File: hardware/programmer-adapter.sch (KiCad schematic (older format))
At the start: 5 parts, among them J2 Target, J3 Conn_ARM_JTAG_SWD_20, U1 AMS1117-3.3

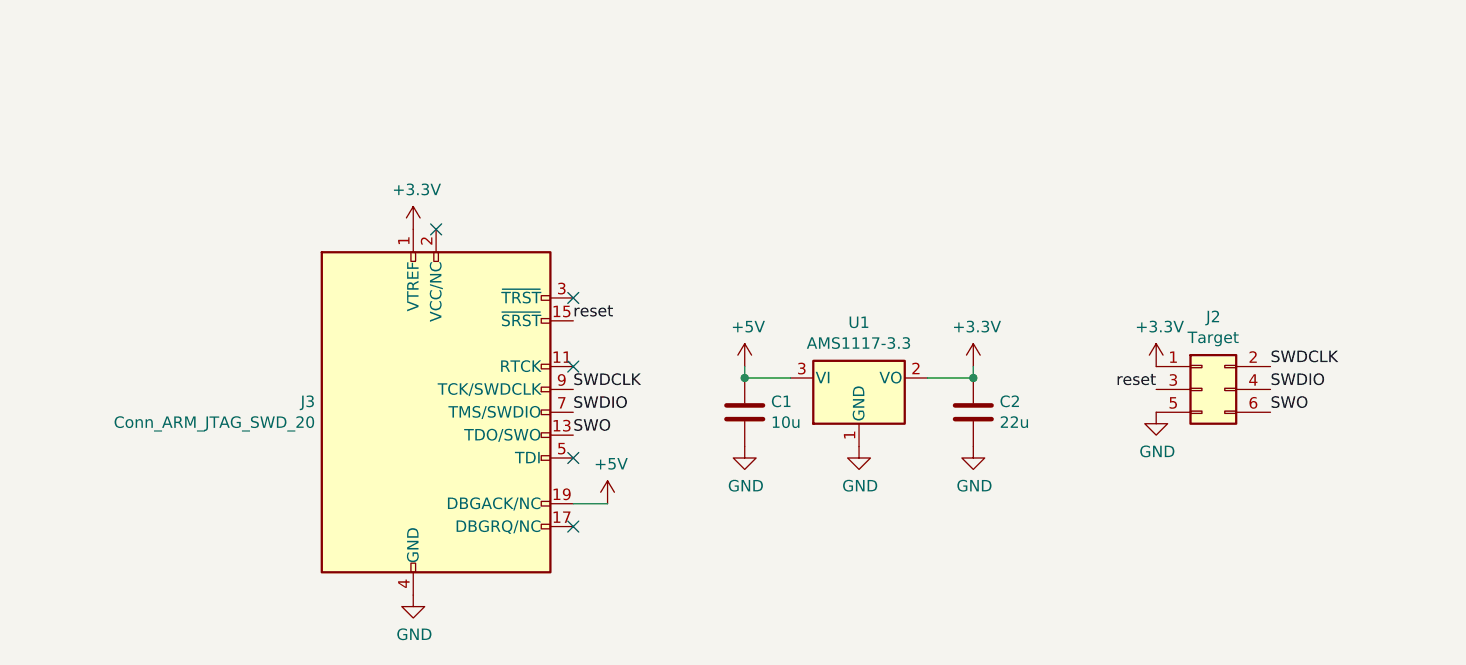
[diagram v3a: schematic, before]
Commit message: Changed LDO to MCP1826S
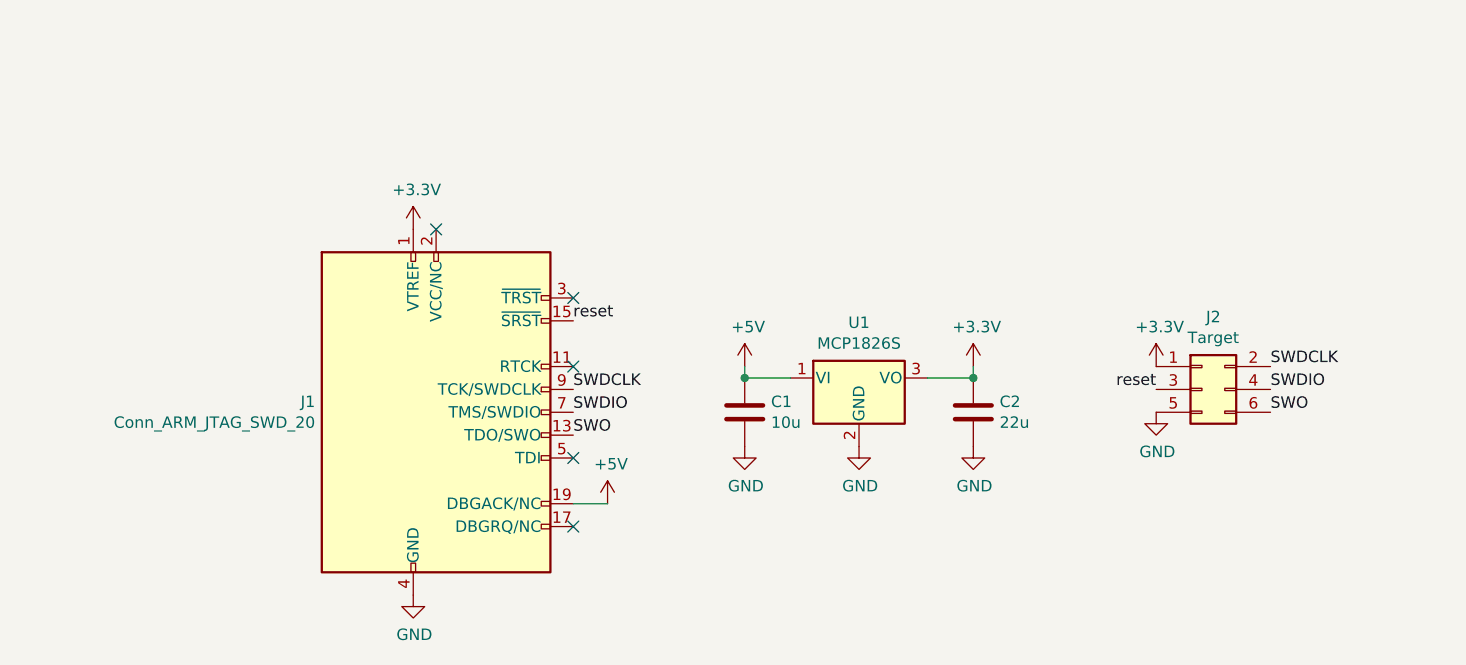
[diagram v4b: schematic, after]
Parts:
- removed U1: AMS1117-3.3, Package_TO_SOT_SMD:SOT-223-3_TabPin2, symbol Regulator_Linear:AMS1117-3.3
- added U1: MCP1826S, Package_TO_SOT_SMD:SOT-223-3_TabPin2, symbol Regulator_Linear:MCP1826S
- renumbered J3 to J1
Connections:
- net +3V3: now also U1.3 (VO)
- net +5V: now also U1.1 (VI)
- net GND: now also U1.2 (GND)
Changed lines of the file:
@@
 Sheet 1 1
 Title "Programmer adapter"
-Date "2020-03-09"
-Rev "1.1.0"
+Date "2020-06-02"
+Rev "1.2.1"
 Comp "Chameleon Electronics "
 Comment1 ""
@@
 $EndDescr
 $Comp
-L Connector:Conn_ARM_JTAG_SWD_20 J3
+L Connector:Conn_ARM_JTAG_SWD_20 J1
 U 1 1 5E4FBF88
 P 4400 4150
-F 0 "J3" H 3871 4196 50  0000 R CNN
+F 0 "J1" H 3871 4196 50  0000 R CNN
 F 1 "Conn_ARM_JTAG_SWD_20" H 3871 4105 50  0000 R CNN
 F 2 "Connector_PinSocket_2.54mm:PinSocket_2x10_P2.54mm_Horizontal" H 4850 3100 50  0001 L TNN
@@
 SWO
 $Comp
-L power:GND #PWR06
+L power:GND #PWR02
 U 1 1 5E4FCD55
 P 4300 4950
-F 0 "#PWR06" H 4300 4700 50  0001 C CNN
+F 0 "#PWR02" H 4300 4700 50  0001 C CNN
 F 1 "GND" H 4305 4777 50  0000 C CNN
 F 2 "" H 4300 4950 50  0001 C CNN
@@
 $EndComp
 $Comp
-L power:+3.3V #PWR03
+L power:+3.3V #PWR09
 U 1 1 5E508EC0
 P 7550 3950
-F 0 "#PWR03" H 7550 3800 50  0001 C CNN
+F 0 "#PWR09" H 7550 3800 50  0001 C CNN
 F 1 "+3.3V" H 7565 4123 50  0000 C CNN
 F 2 "" H 7550 3950 50  0001 C CNN
@@
 $EndComp
 $Comp
-L power:GND #PWR05
+L power:GND #PWR010
 U 1 1 5E5092F6
 P 7550 4150
-F 0 "#PWR05" H 7550 3900 50  0001 C CNN
+F 0 "#PWR010" H 7550 3900 50  0001 C CNN
 F 1 "GND" H 7555 3977 50  0000 C CNN
 F 2 "" H 7550 4150 50  0001 C CNN
@@
 reset
 $Comp
-L Regulator_Linear:AMS1117-3.3 U1
-U 1 1 5ED5B523
-P 6250 4000
-F 0 "U1" H 6250 4242 50  0000 C CNN
-F 1 "AMS1117-3.3" H 6250 4151 50  0000 C CNN
-F 2 "Package_TO_SOT_SMD:SOT-223-3_TabPin2" H 6250 4200 50  0001 C CNN
-F 3 "http://www.advanced-monolithic.com/pdf/ds1117.pdf" H 6350 3750 50  0001 C CNN
-	1    6250 4000
-	1    0    0    -1
-$EndComp
-$Comp
-L power:+5V #PWR0101
+L power:+5V #PWR03
 U 1 1 5ED5BE1C
 P 5150 4550
-F 0 "#PWR0101" H 5150 4400 50  0001 C CNN
+F 0 "#PWR03" H 5150 4400 50  0001 C CNN
 F 1 "+5V" H 5165 4723 50  0000 C CNN
 F 2 "" H 5150 4550 50  0001 C CNN
@@
 $EndComp
 $Comp
-L power:+5V #PWR0102
+L power:+5V #PWR04
 U 1 1 5ED5E701
 P 5750 3950
-F 0 "#PWR0102" H 5750 3800 50  0001 C CNN
+F 0 "#PWR04" H 5750 3800 50  0001 C CNN
 F 1 "+5V" H 5765 4123 50  0000 C CNN
 F 2 "" H 5750 3950 50  0001 C CNN
@@
 	5750 4000 5950 4000
 $Comp
-L power:GND #PWR0103
+L power:GND #PWR06
 U 1 1 5ED5EF4A
 P 6250 4300
-F 0 "#PWR0103" H 6250 4050 50  0001 C CNN
+F 0 "#PWR06" H 6250 4050 50  0001 C CNN
 F 1 "GND" H 6255 4127 50  0000 C CNN
 F 2 "" H 6250 4300 50  0001 C CNN
@@
 $EndComp
 $Comp
-L power:+3.3V #PWR0104
+L power:+3.3V #PWR07
 U 1 1 5ED5F3AA
 P 6750 3950
-F 0 "#PWR0104" H 6750 3800 50  0001 C CNN
+F 0 "#PWR07" H 6750 3800 50  0001 C CNN
 F 1 "+3.3V" H 6765 4123 50  0000 C CNN
 F 2 "" H 6750 3950 50  0001 C CNN
@@
 Connection ~ 6750 4000
 $Comp
-L power:GND #PWR0105
+L power:GND #PWR05
 U 1 1 5ED69C3E
 P 5750 4300
-F 0 "#PWR0105" H 5750 4050 50  0001 C CNN
+F 0 "#PWR05" H 5750 4050 50  0001 C CNN
 F 1 "GND" H 5755 4127 50  0000 C CNN
 F 2 "" H 5750 4300 50  0001 C CNN
@@
 $EndComp
 $Comp
-L power:GND #PWR0106
+L power:GND #PWR08
 U 1 1 5ED69F09
 P 6750 4300
-F 0 "#PWR0106" H 6750 4050 50  0001 C CNN
+F 0 "#PWR08" H 6750 4050 50  0001 C CNN
 F 1 "GND" H 6755 4127 50  0000 C CNN
 F 2 "" H 6750 4300 50  0001 C CNN
@@
 	5150 4550 5000 4550
 NoConn ~ 4400 3350
+$Comp
+L Regulator_Linear:MCP1826S U1
+U 1 1 5ED64636
+P 6250 4000
+F 0 "U1" H 6250 4242 50  0000 C CNN
+F 1 "MCP1826S" H 6250 4151 50  0000 C CNN
+F 2 "Package_TO_SOT_SMD:SOT-223-3_TabPin2" H 6150 4150 50  0001 C CNN
+F 3 "http://ww1.microchip.com/downloads/en/DeviceDoc/22057B.pdf" H 6250 4250 50  0001 C CNN
+	1    6250 4000
+	1    0    0    -1
+$EndComp
 $EndSCHEMATC

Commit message: VCOM connection
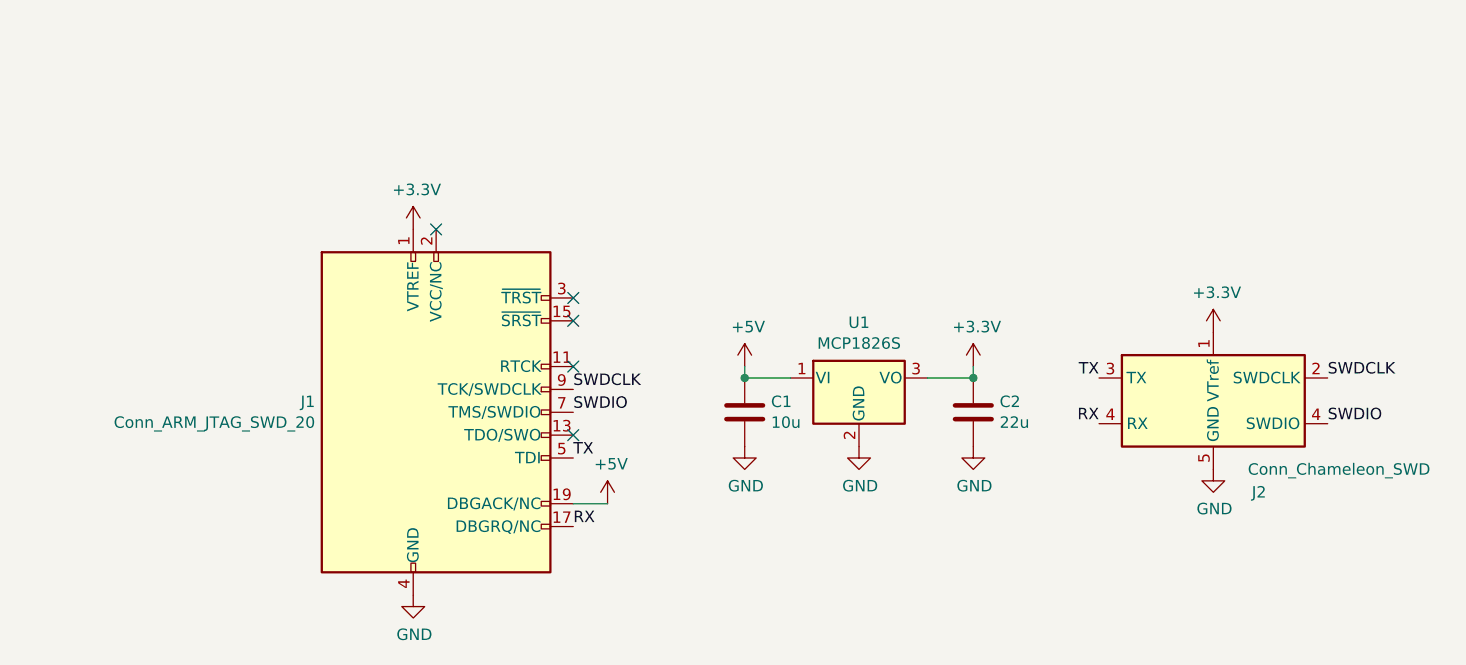
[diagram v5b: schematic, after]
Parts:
- removed J2: Target, Connector_PinHeader_1.27mm:PinHeader_2x03_P1.27mm_Vertical_SMD, symbol Connector_Generic:Conn_02x03_Odd_Even
- added J2: Conn_Chameleon_SWD, IoT_Home:Chameleon_SWD_Header, symbol IoT_Home:Conn_Chameleon_SWD
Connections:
- net +3V3: now also J2.1 (VTref)
- net GND: now also J2.5 (GND)
- net SWDCLK: now also J2.2 (SWDCLK)
- net SWDIO: now also J2.4 (SWDIO)
- net RX: now reaches J1.17 (DBGRQ/NC)
- net RX: now also J2.4 (SWDIO)
- net TX: now reaches J1.5 (TDI)
- net TX: now also J2.3 (TX)
- net SWO: no longer names the net of J1.13 (TDO/SWO)
- net reset: no longer names the net of J1.15 (~SRST~)
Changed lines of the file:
@@
 Comment4 ""
 $EndDescr
+Text Label 5000 4150 0    50   ~ 0
+SWDIO
+Text Label 5000 4050 0    50   ~ 0
+SWDCLK
+$Comp
+L power:GND #PWR02
+U 1 1 5E4FCD55
+P 4300 4950
+F 0 "#PWR02" H 4300 4700 50  0001 C CNN
+F 1 "GND" H 4305 4777 50  0000 C CNN
+F 2 "" H 4300 4950 50  0001 C CNN
+F 3 "" H 4300 4950 50  0001 C CNN
+	1    4300 4950
+	1    0    0    -1
+$EndComp
+NoConn ~ 5000 3650
+NoConn ~ 5000 3950
+$Comp
+L power:+3.3V #PWR01
+U 1 1 5E4FE2E4
+P 4300 3350
+F 0 "#PWR01" H 4300 3200 50  0001 C CNN
+F 1 "+3.3V" H 4315 3523 50  0000 C CNN
+F 2 "" H 4300 3350 50  0001 C CNN
+F 3 "" H 4300 3350 50  0001 C CNN
+	1    4300 3350
+	1    0    0    -1
+$EndComp
+$Comp
+L power:+3.3V #PWR09
+U 1 1 5E508EC0
+P 7800 3800
+F 0 "#PWR09" H 7800 3650 50  0001 C CNN
+F 1 "+3.3V" H 7815 3973 50  0000 C CNN
+F 2 "" H 7800 3800 50  0001 C CNN
+F 3 "" H 7800 3800 50  0001 C CNN
+	1    7800 3800
+	1    0    0    -1
+$EndComp
+$Comp
+L power:GND #PWR010
+U 1 1 5E5092F6
+P 7800 4400
+F 0 "#PWR010" H 7800 4150 50  0001 C CNN
+F 1 "GND" H 7805 4227 50  0000 C CNN
+F 2 "" H 7800 4400 50  0001 C CNN
+F 3 "" H 7800 4400 50  0001 C CNN
+	1    7800 4400
+	1    0    0    -1
+$EndComp
+Text Label 8300 4200 0    50   ~ 0
+SWDIO
+Text Label 8300 4000 0    50   ~ 0
+SWDCLK
+$Comp
+L power:+5V #PWR03
+U 1 1 5ED5BE1C
+P 5150 4550
+F 0 "#PWR03" H 5150 4400 50  0001 C CNN
+F 1 "+5V" H 5165 4723 50  0000 C CNN
+F 2 "" H 5150 4550 50  0001 C CNN
+F 3 "" H 5150 4550 50  0001 C CNN
+	1    5150 4550
+	1    0    0    -1
+$EndComp
+$Comp
+L power:+5V #PWR04
+U 1 1 5ED5E701
+P 5750 3950
+F 0 "#PWR04" H 5750 3800 50  0001 C CNN
+F 1 "+5V" H 5765 4123 50  0000 C CNN
+F 2 "" H 5750 3950 50  0001 C CNN
+F 3 "" H 5750 3950 50  0001 C CNN
+	1    5750 3950
+	1    0    0    -1
+$EndComp
+Wire Wire Line
+	5750 3950 5750 4000
+Wire Wire Line
+	5750 4000 5950 4000
+$Comp
+L power:GND #PWR06
+U 1 1 5ED5EF4A
+P 6250 4300
+F 0 "#PWR06" H 6250 4050 50  0001 C CNN
+F 1 "GND" H 6255 4127 50  0000 C CNN
+F 2 "" H 6250 4300 50  0001 C CNN
+F 3 "" H 6250 4300 50  0001 C CNN
+	1    6250 4300
+	1    0    0    -1
+$EndComp
+$Comp
+L power:+3.3V #PWR07
+U 1 1 5ED5F3AA
+P 6750 3950
+F 0 "#PWR07" H 6750 3800 50  0001 C CNN
+F 1 "+3.3V" H 6765 4123 50  0000 C CNN
+F 2 "" H 6750 3950 50  0001 C CNN
+F 3 "" H 6750 3950 50  0001 C CNN
+	1    6750 3950
+	1    0    0    -1
+$EndComp
+Wire Wire Line
+	6750 3950 6750 4000
+Wire Wire Line
+	6750 4000 6550 4000
+$Comp
+L Device:C C1
+U 1 1 5ED6736D
+P 5750 4150
+F 0 "C1" H 5865 4196 50  0000 L CNN
+F 1 "10u" H 5865 4105 50  0000 L CNN
+F 2 "Capacitor_SMD:C_0805_2012Metric" H 5788 4000 50  0001 C CNN
+F 3 "~" H 5750 4150 50  0001 C CNN
+	1    5750 4150
+	1    0    0    -1
+$EndComp
+Connection ~ 5750 4000
+$Comp
+L Device:C C2
+U 1 1 5ED697B9
+P 6750 4150
+F 0 "C2" H 6865 4196 50  0000 L CNN
+F 1 "22u" H 6865 4105 50  0000 L CNN
+F 2 "Capacitor_SMD:C_0805_2012Metric" H 6788 4000 50  0001 C CNN
+F 3 "~" H 6750 4150 50  0001 C CNN
+	1    6750 4150
+	1    0    0    -1
+$EndComp
+Connection ~ 6750 4000
+$Comp
+L power:GND #PWR05
+U 1 1 5ED69C3E
+P 5750 4300
+F 0 "#PWR05" H 5750 4050 50  0001 C CNN
+F 1 "GND" H 5755 4127 50  0000 C CNN
+F 2 "" H 5750 4300 50  0001 C CNN
+F 3 "" H 5750 4300 50  0001 C CNN
+	1    5750 4300
+	1    0    0    -1
+$EndComp
+$Comp
+L power:GND #PWR08
+U 1 1 5ED69F09
+P 6750 4300
+F 0 "#PWR08" H 6750 4050 50  0001 C CNN
+F 1 "GND" H 6755 4127 50  0000 C CNN
+F 2 "" H 6750 4300 50  0001 C CNN
+F 3 "" H 6750 4300 50  0001 C CNN
+	1    6750 4300
+	1    0    0    -1
+$EndComp
+Wire Wire Line
+	5150 4550 5000 4550
+NoConn ~ 4400 3350
+$Comp
+L Regulator_Linear:MCP1826S U1
+U 1 1 5ED64636
+P 6250 4000
+F 0 "U1" H 6250 4242 50  0000 C CNN
+F 1 "MCP1826S" H 6250 4151 50  0000 C CNN
+F 2 "Package_TO_SOT_SMD:SOT-223-3_TabPin2" H 6150 4150 50  0001 C CNN
+F 3 "http://ww1.microchip.com/downloads/en/DeviceDoc/22057B.pdf" H 6250 4250 50  0001 C CNN
+	1    6250 4000
+	1    0    0    -1
+$EndComp
+$Comp
+L IoT_Home:Conn_Chameleon_SWD J2
+U 1 1 5F02051F
+P 7800 4100
+F 0 "J2" H 8000 3700 50  0000 C CNN
+F 1 "Conn_Chameleon_SWD" H 8350 3800 50  0000 C CNN
+F 2 "IoT_Home:Chameleon_SWD_Header" H 7800 3800 50  0001 C CNN
+F 3 "https://github.com/Chameleon-Electronics/programmer-adapter" V 7450 2850 50  0001 C CNN
+	1    7800 4100
+	1    0    0    -1
+$EndComp
+Text Label 7300 4000 2    50   ~ 0
+TX
+Text Label 7300 4200 2    50   ~ 0
+RX
+NoConn ~ 5000 3750
+NoConn ~ 5000 4250
+Text Label 5000 4350 0    50   ~ 0
+TX
 $Comp
 L Connector:Conn_ARM_JTAG_SWD_20 J1
@@
 	1    0    0    -1
 $EndComp
-Text Label 5000 4150 0    50   ~ 0
-SWDIO
-Text Label 5000 4050 0    50   ~ 0
-SWDCLK
-Text Label 5000 4250 0    50   ~ 0
-SWO
-$Comp
-L power:GND #PWR02
-U 1 1 5E4FCD55
-P 4300 4950
-F 0 "#PWR02" H 4300 4700 50  0001 C CNN
-F 1 "GND" H 4305 4777 50  0000 C CNN
-F 2 "" H 4300 4950 50  0001 C CNN
-F 3 "" H 4300 4950 50  0001 C CNN
-	1    4300 4950
-	1    0    0    -1
-$EndComp
-NoConn ~ 5000 3650
-NoConn ~ 5000 3950
-NoConn ~ 5000 4350
-NoConn ~ 5000 4650
-$Comp
-L power:+3.3V #PWR01
-U 1 1 5E4FE2E4
-P 4300 3350
-F 0 "#PWR01" H 4300 3200 50  0001 C CNN
-F 1 "+3.3V" H 4315 3523 50  0000 C CNN
-F 2 "" H 4300 3350 50  0001 C CNN
-F 3 "" H 4300 3350 50  0001 C CNN
-	1    4300 3350
-	1    0    0    -1
-$EndComp
-$Comp
-L Connector_Generic:Conn_02x03_Odd_Even J2
-U 1 1 5E501B04
-P 7750 4050
-F 0 "J2" H 7800 4367 50  0000 C CNN
-F 1 "Target" H 7800 4276 50  0000 C CNN
-F 2 "Connector_PinHeader_1.27mm:PinHeader_2x03_P1.27mm_Vertical_SMD" H 7750 4050 50  0001 C CNN
-F 3 "~" H 7750 4050 50  0001 C CNN
-	1    7750 4050
-	1    0    0    -1
-$EndComp
-$Comp
-L power:+3.3V #PWR09
-U 1 1 5E508EC0
-P 7550 3950
-F 0 "#PWR09" H 7550 3800 50  0001 C CNN
-F 1 "+3.3V" H 7565 4123 50  0000 C CNN
-F 2 "" H 7550 3950 50  0001 C CNN
-F 3 "" H 7550 3950 50  0001 C CNN
-	1    7550 3950
-	1    0    0    -1
-$EndComp
-$Comp
-L power:GND #PWR010
-U 1 1 5E5092F6
-P 7550 4150
-F 0 "#PWR010" H 7550 3900 50  0001 C CNN
-F 1 "GND" H 7555 3977 50  0000 C CNN
-F 2 "" H 7550 4150 50  0001 C CNN
-F 3 "" H 7550 4150 50  0001 C CNN
-	1    7550 4150
-	1    0    0    -1
-$EndComp
-Text Label 8050 4050 0    50   ~ 0
-SWDIO
-Text Label 8050 3950 0    50   ~ 0
-SWDCLK
-Text Label 8050 4150 0    50   ~ 0
-SWO
-Text Label 5000 3750 0    50   ~ 0
-reset
-Text Label 7550 4050 2    50   ~ 0
-reset
-$Comp
-L power:+5V #PWR03
-U 1 1 5ED5BE1C
-P 5150 4550
-F 0 "#PWR03" H 5150 4400 50  0001 C CNN
-F 1 "+5V" H 5165 4723 50  0000 C CNN
-F 2 "" H 5150 4550 50  0001 C CNN
-F 3 "" H 5150 4550 50  0001 C CNN
-	1    5150 4550
-	1    0    0    -1
-$EndComp
-$Comp
-L power:+5V #PWR04
-U 1 1 5ED5E701
-P 5750 3950
-F 0 "#PWR04" H 5750 3800 50  0001 C CNN
-F 1 "+5V" H 5765 4123 50  0000 C CNN
-F 2 "" H 5750 3950 50  0001 C CNN
-F 3 "" H 5750 3950 50  0001 C CNN
-	1    5750 3950
-	1    0    0    -1
-$EndComp
-Wire Wire Line
-	5750 3950 5750 4000
-Wire Wire Line
-	5750 4000 5950 4000
-$Comp
-L power:GND #PWR06
-U 1 1 5ED5EF4A
-P 6250 4300
-F 0 "#PWR06" H 6250 4050 50  0001 C CNN
-F 1 "GND" H 6255 4127 50  0000 C CNN
-F 2 "" H 6250 4300 50  0001 C CNN
-F 3 "" H 6250 4300 50  0001 C CNN
-	1    6250 4300
-	1    0    0    -1
-$EndComp
-$Comp
-L power:+3.3V #PWR07
-U 1 1 5ED5F3AA
-P 6750 3950
-F 0 "#PWR07" H 6750 3800 50  0001 C CNN
-F 1 "+3.3V" H 6765 4123 50  0000 C CNN
-F 2 "" H 6750 3950 50  0001 C CNN
-F 3 "" H 6750 3950 50  0001 C CNN
-	1    6750 3950
-	1    0    0    -1
-$EndComp
-Wire Wire Line
-	6750 3950 6750 4000
-Wire Wire Line
-	6750 4000 6550 4000
-$Comp
-L Device:C C1
-U 1 1 5ED6736D
-P 5750 4150
-F 0 "C1" H 5865 4196 50  0000 L CNN
-F 1 "10u" H 5865 4105 50  0000 L CNN
-F 2 "Capacitor_SMD:C_0805_2012Metric" H 5788 4000 50  0001 C CNN
-F 3 "~" H 5750 4150 50  0001 C CNN
-	1    5750 4150
-	1    0    0    -1
-$EndComp
-Connection ~ 5750 4000
-$Comp
-L Device:C C2
-U 1 1 5ED697B9
-P 6750 4150
-F 0 "C2" H 6865 4196 50  0000 L CNN
-F 1 "22u" H 6865 4105 50  0000 L CNN
-F 2 "Capacitor_SMD:C_0805_2012Metric" H 6788 4000 50  0001 C CNN
-F 3 "~" H 6750 4150 50  0001 C CNN
-	1    6750 4150
-	1    0    0    -1
-$EndComp
-Connection ~ 6750 4000
-$Comp
-L power:GND #PWR05
-U 1 1 5ED69C3E
-P 5750 4300
-F 0 "#PWR05" H 5750 4050 50  0001 C CNN
-F 1 "GND" H 5755 4127 50  0000 C CNN
-F 2 "" H 5750 4300 50  0001 C CNN
-F 3 "" H 5750 4300 50  0001 C CNN
-	1    5750 4300
-	1    0    0    -1
-$EndComp
-$Comp
-L power:GND #PWR08
-U 1 1 5ED69F09
-P 6750 4300
-F 0 "#PWR08" H 6750 4050 50  0001 C CNN
-F 1 "GND" H 6755 4127 50  0000 C CNN
-F 2 "" H 6750 4300 50  0001 C CNN
-F 3 "" H 6750 4300 50  0001 C CNN
-	1    6750 4300
-	1    0    0    -1
-$EndComp
-Wire Wire Line
-	5150 4550 5000 4550
-NoConn ~ 4400 3350
-$Comp
-L Regulator_Linear:MCP1826S U1
-U 1 1 5ED64636
-P 6250 4000
-F 0 "U1" H 6250 4242 50  0000 C CNN
-F 1 "MCP1826S" H 6250 4151 50  0000 C CNN
-F 2 "Package_TO_SOT_SMD:SOT-223-3_TabPin2" H 6150 4150 50  0001 C CNN
-F 3 "http://ww1.microchip.com/downloads/en/DeviceDoc/22057B.pdf" H 6250 4250 50  0001 C CNN
-	1    6250 4000
-	1    0    0    -1
-$EndComp
+Text Label 5000 4650 0    50   ~ 0
+RX
 $EndSCHEMATC
